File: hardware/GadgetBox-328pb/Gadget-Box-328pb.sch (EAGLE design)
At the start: 34 parts, among them IC1A ATMEGA328PB-AU, IC1B ATMEGA328PB-MU, U1 MCP73831T-2ACI/OT, U2 AP2112-3.3, X1 CRYSTAL-0500290P1

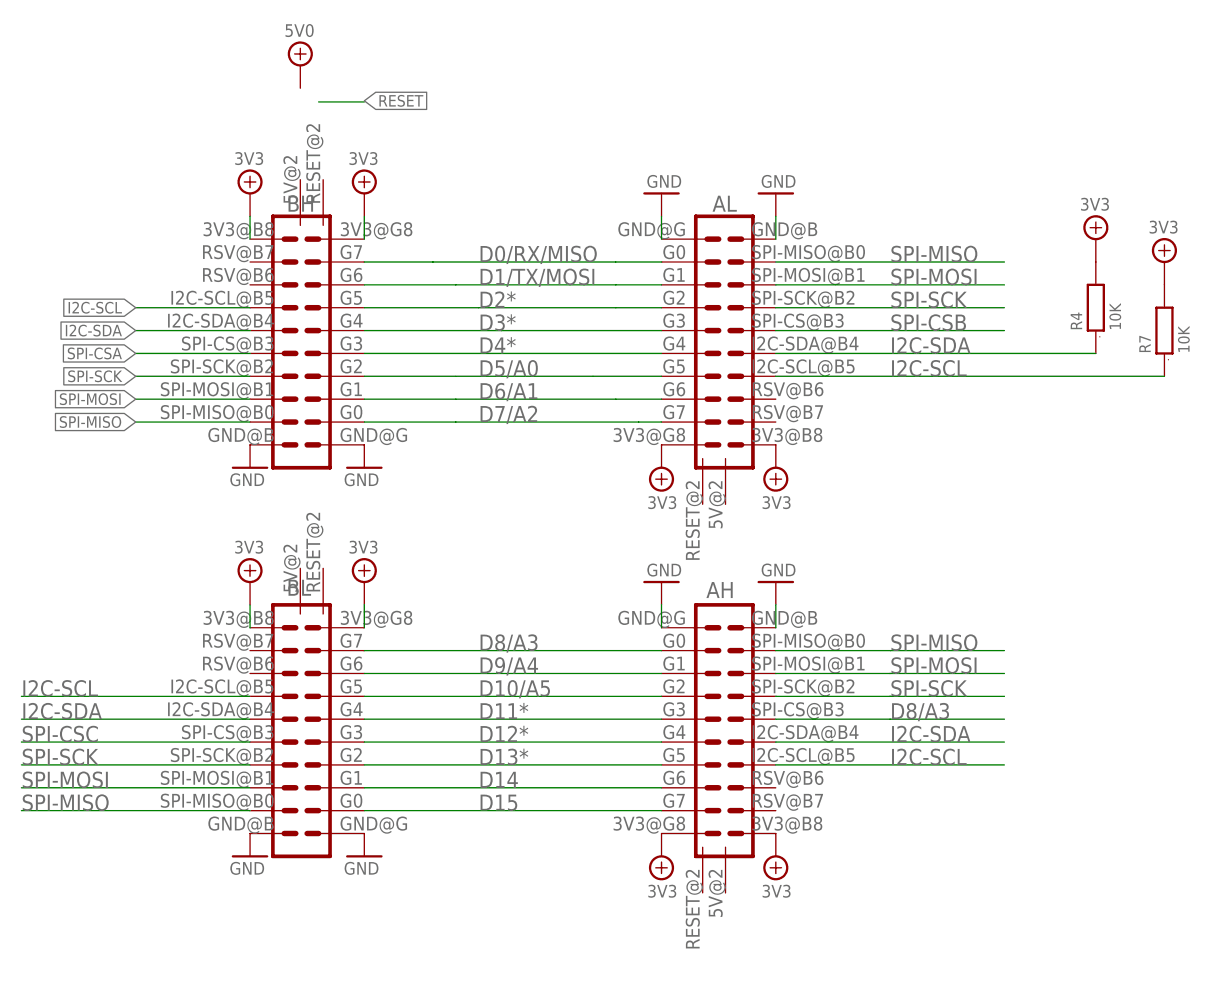
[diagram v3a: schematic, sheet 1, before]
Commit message: updated eCog connectors to newer version footprint
finor rerouting and other minor repair of an airwire
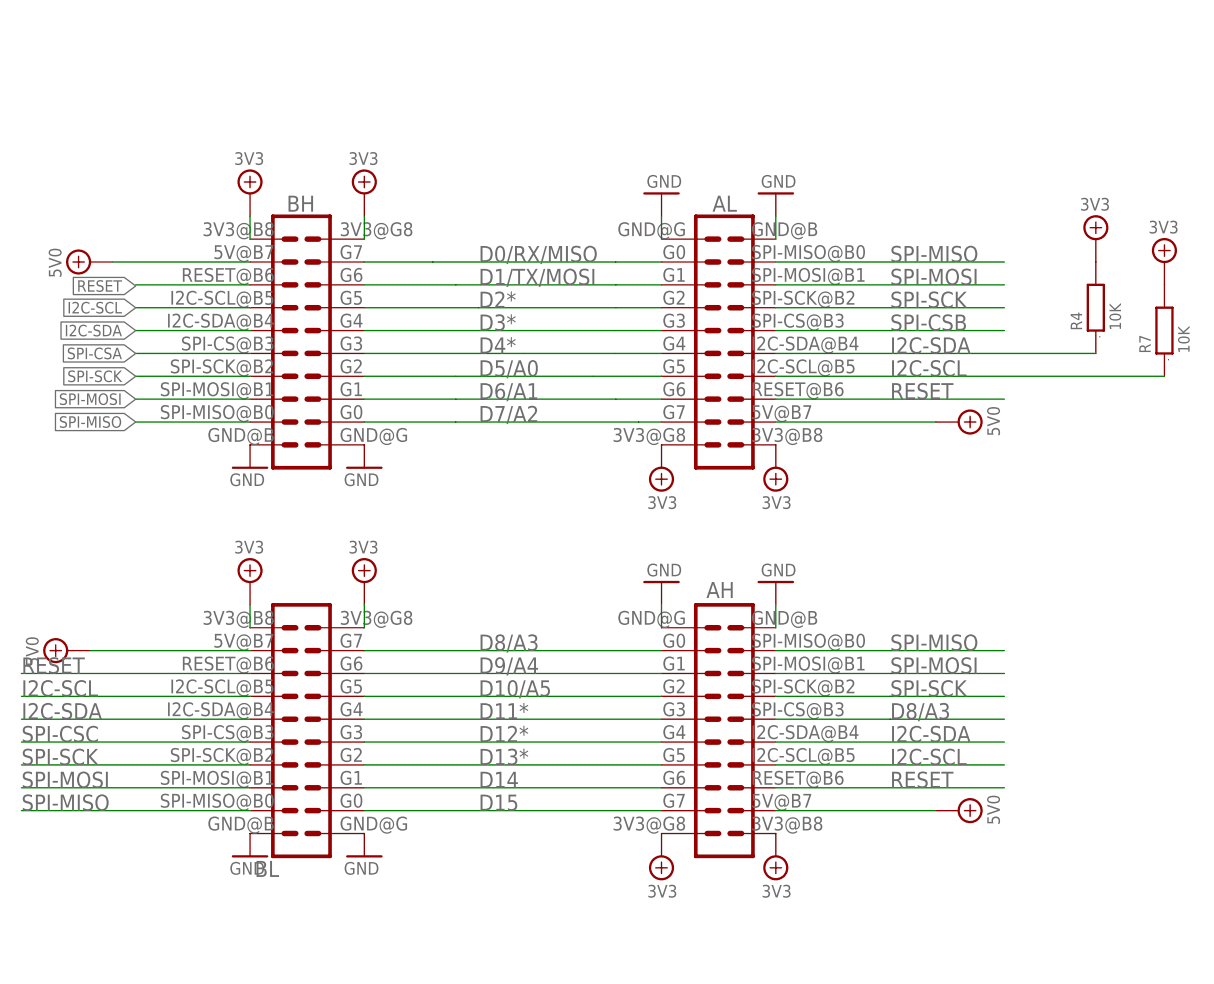
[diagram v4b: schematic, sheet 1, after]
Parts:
- AH, AL, BH, BL: value ECOGECOG_SLOT_ALT1 -> ECOGECOG_SLOT; device eCogs:ECOGECOG_SLOT_ALT1 -> eCogs:ECOGECOG_SLOT
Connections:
- net 5V0: now also AH.5V@B7, AL.5V@B7, BH.5V@B7, BL.5V@B7
- net RESET: now also AH.RESET@B6, AL.RESET@B6, BH.RESET@B6, BL.RESET@B6
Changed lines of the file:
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@@
 <part name="3V3_PWR16" library="GadgetFactory" deviceset="3V3" device=""/>
 <part name="3V3_PWR18" library="GadgetFactory" deviceset="3V3" device=""/>
-<part name="BH" library="eCogs" deviceset="ECOG" device="ECOG_SLOT_ALT1" value="ECOGECOG_SLOT_ALT1">
+<part name="BH" library="eCogs" deviceset="ECOG" device="ECOG_SLOT" value="ECOGECOG_SLOT">
 <attribute name="PARTNO" value="PPPC102LFBN-RC,SULLINS CONNECTOR SOLUTIONS,dk,S6106-ND,&quot;CONN HEADER FEM 20POS.1&quot;&quot; DL GOLD&quot;, REF67"/>
 </part>
-<part name="AL" library="eCogs" deviceset="ECOG" device="ECOG_SLOT_ALT1" value="ECOGECOG_SLOT_ALT1">
+<part name="AL" library="eCogs" deviceset="ECOG" device="ECOG_SLOT" value="ECOGECOG_SLOT">
 <attribute name="PARTNO" value="PPPC102LFBN-RC,SULLINS CONNECTOR SOLUTIONS,dk,S6106-ND,&quot;CONN HEADER FEM 20POS.1&quot;&quot; DL GOLD&quot;, REF67"/>
 </part>
-<part name="AH" library="eCogs" deviceset="ECOG" device="ECOG_SLOT_ALT1" value="ECOGECOG_SLOT_ALT1">
+<part name="AH" library="eCogs" deviceset="ECOG" device="ECOG_SLOT" value="ECOGECOG_SLOT">
 <attribute name="PARTNO" value="PPPC102LFBN-RC,SULLINS CONNECTOR SOLUTIONS,dk,S6106-ND,&quot;CONN HEADER FEM 20POS.1&quot;&quot; DL GOLD&quot;, REF67"/>
 </part>
-<part name="BL" library="eCogs" deviceset="ECOG" device="ECOG_SLOT_ALT1" value="ECOGECOG_SLOT_ALT1">
+<part name="BL" library="eCogs" deviceset="ECOG" device="ECOG_SLOT" value="ECOGECOG_SLOT">
 <attribute name="PARTNO" value="PPPC102LFBN-RC,SULLINS CONNECTOR SOLUTIONS,dk,S6106-ND,&quot;CONN HEADER FEM 20POS.1&quot;&quot; DL GOLD&quot;, REF67"/>
 </part>
@@
 <part name="U$1" library="microbuilder" deviceset="VBUS" device=""/>
 <part name="U$5" library="microbuilder" deviceset="GND" device=""/>
+<part name="5V0_PWR1" library="GadgetFactory" deviceset="5V0" device=""/>
+<part name="5V0_PWR3" library="GadgetFactory" deviceset="5V0" device=""/>
+<part name="5V0_PWR4" library="GadgetFactory" deviceset="5V0" device=""/>
 </parts>
 <sheets>
@@
 <attribute name="PARTNO" x="152.4" y="63.5" size="1.778" layer="96" display="off"/>
 </instance>
-<instance part="BL" gate="ECOG$1" x="104.14" y="35.56" smashed="yes">
-<attribute name="NAME" x="103.124" y="64.516" size="1.778" layer="95"/>
+<instance part="BL" gate="ECOG$1" x="104.14" y="35.56">
 <attribute name="PARTNO" x="104.14" y="35.56" size="1.778" layer="96" display="off"/>
 </instance>
@@
 <instance part="GND9" gate="A" x="157.48" y="66.04" rot="R180"/>
 <instance part="3V3_PWR9" gate="A" x="111.76" y="109.22"/>
-<instance part="5V0_PWR2" gate="A" x="104.648" y="123.444"/>
+<instance part="5V0_PWR2" gate="A" x="81.28" y="101.6" rot="R90"/>
 <instance part="R4" gate="A" x="193.04" y="96.52" rot="R90">
 <attribute name="PARTNO" x="193.04" y="96.52" size="1.778" layer="96" display="off"/>
@@
 <instance part="3V3_PWR1" gate="A" x="193.04" y="104.14"/>
 <instance part="3V3_PWR2" gate="A" x="200.66" y="101.6"/>
+<instance part="5V0_PWR1" gate="A" x="78.74" y="58.42" rot="R90"/>
+<instance part="5V0_PWR3" gate="A" x="177.8" y="83.82" rot="R270"/>
+<instance part="5V0_PWR4" gate="A" x="177.8" y="40.64" rot="R270"/>
 </instances>
 <busses>
@@
 <net name="RESET" class="0">
 <segment>
-<label x="111.76" y="119.507" size="1.27" layer="95" xref="yes"/>
-<wire x1="106.68" y1="119.38" x2="111.76" y2="119.38" width="0.2032" layer="91"/>
+<label x="86.36" y="98.933" size="1.27" layer="95" rot="R180" xref="yes"/>
+<wire x1="86.36" y1="99.06" x2="99.06" y2="99.06" width="0.2032" layer="91"/>
+<pinref part="BH" gate="ECOG$1" pin="RESET@B6"/>
+</segment>
+<segment>
+<wire x1="157.48" y1="86.36" x2="182.88" y2="86.36" width="0.2032" layer="91"/>
+<pinref part="AL" gate="ECOG$1" pin="RESET@B6"/>
+<label x="170.18" y="86.36" size="1.778" layer="95"/>
+</segment>
+<segment>
+<wire x1="157.48" y1="43.18" x2="182.88" y2="43.18" width="0.2032" layer="91"/>
+<pinref part="AH" gate="ECOG$1" pin="RESET@B6"/>
+<label x="170.18" y="43.18" size="1.778" layer="95"/>
+</segment>
+<segment>
+<wire x1="73.66" y1="55.88" x2="99.06" y2="55.88" width="0.2032" layer="91"/>
+<pinref part="BL" gate="ECOG$1" pin="RESET@B6"/>
+<label x="73.66" y="55.88" size="1.778" layer="95"/>
 </segment>
 </net>
@@
 </segment>
 </net>
+<net name="5V0" class="0">
+<segment>
+<pinref part="BH" gate="ECOG$1" pin="5V@B7"/>
+<pinref part="5V0_PWR2" gate="A" pin="5V0"/>
+<wire x1="83.82" y1="101.6" x2="99.06" y2="101.6" width="0.1524" layer="91"/>
+</segment>
+<segment>
+<pinref part="BL" gate="ECOG$1" pin="5V@B7"/>
+<pinref part="5V0_PWR1" gate="A" pin="5V0"/>
+<wire x1="81.28" y1="58.42" x2="99.06" y2="58.42" width="0.1524" layer="91"/>
+</segment>
+<segment>
+<pinref part="AL" gate="ECOG$1" pin="5V@B7"/>
+<pinref part="5V0_PWR3" gate="A" pin="5V0"/>
+<wire x1="175.26" y1="83.82" x2="157.48" y2="83.82" width="0.1524" layer="91"/>
+</segment>
+<segment>
+<pinref part="AH" gate="ECOG$1" pin="5V@B7"/>
+<pinref part="5V0_PWR4" gate="A" pin="5V0"/>
+<wire x1="175.26" y1="40.64" x2="157.48" y2="40.64" width="0.1524" layer="91"/>
+</segment>
+</net>
